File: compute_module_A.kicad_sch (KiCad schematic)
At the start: 4 parts, among them J1 Micro_SD_Card_Det

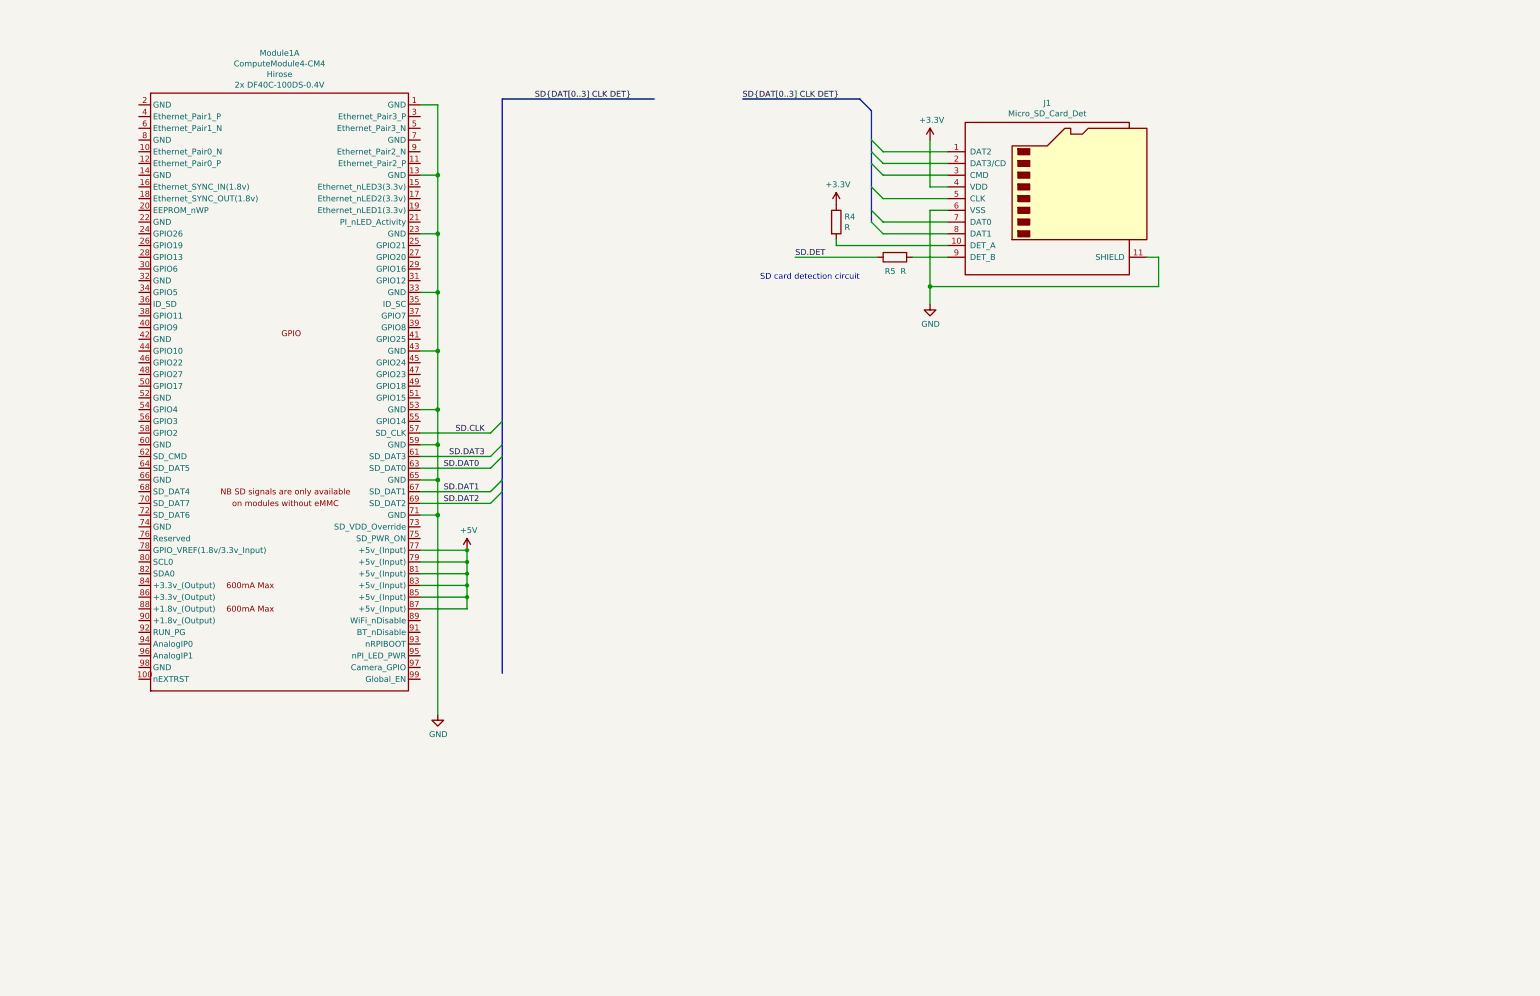
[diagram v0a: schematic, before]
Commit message: Added buses and USB ports to schematic
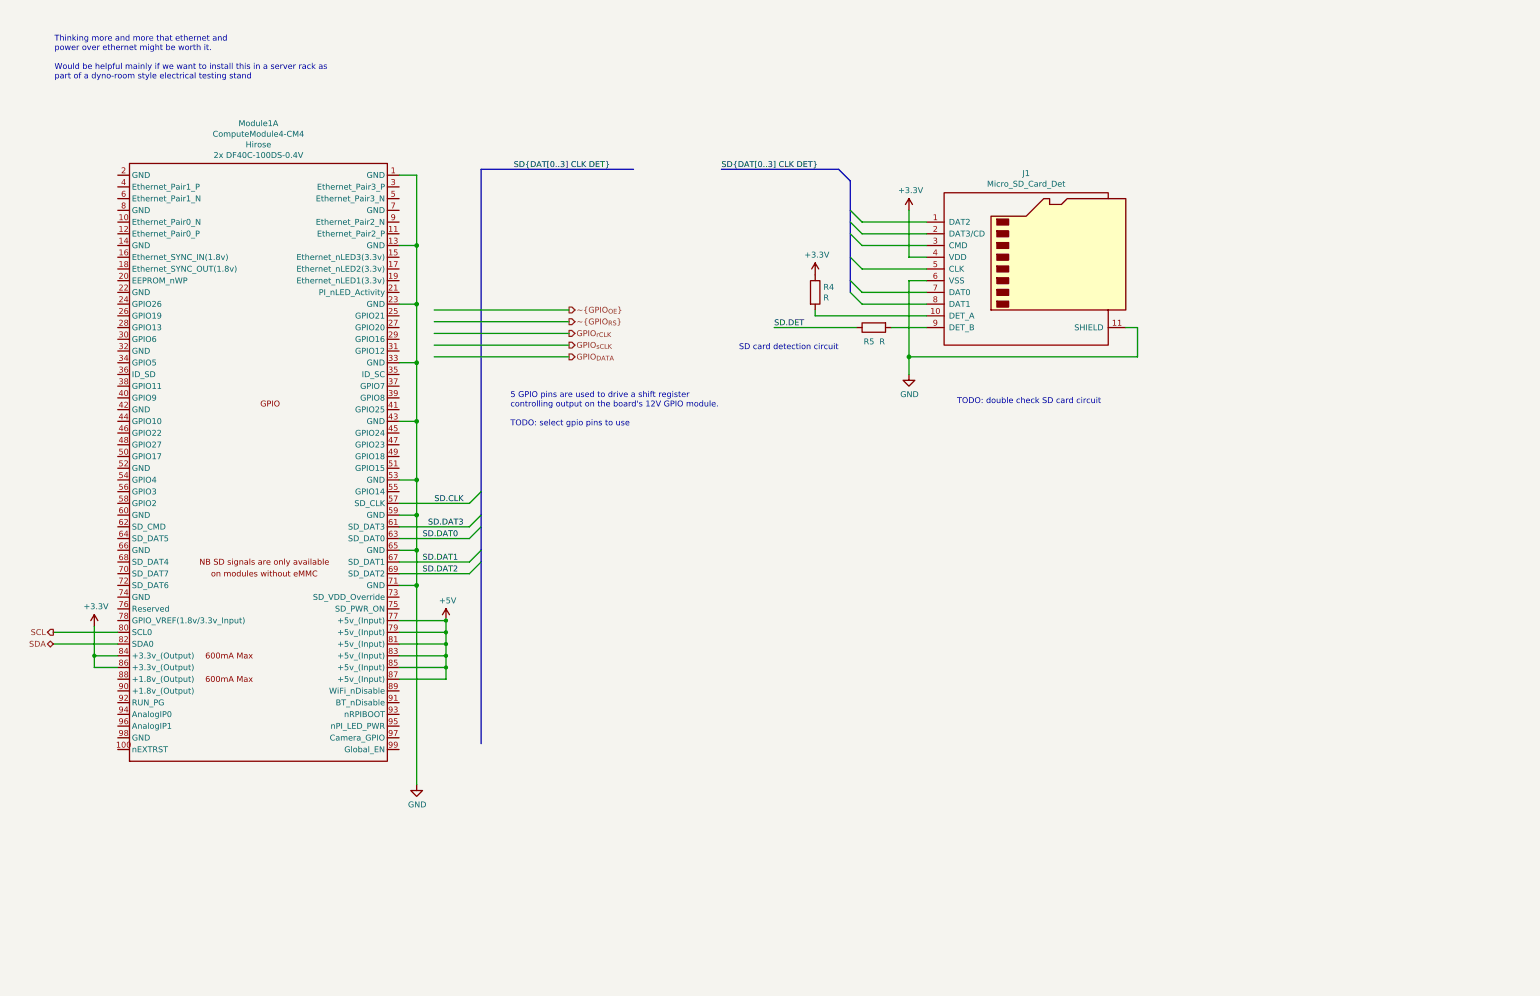
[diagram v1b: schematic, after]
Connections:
- net +3V3: now also Module1.84 (+3.3v_(Output)), Module1.86 (+3.3v_(Output))
- net SCL: now reaches Module1.80 (SCL0)
- net SDA: now reaches Module1.82 (SDA0)
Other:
- note added: "5 GPIO pins are used to drive a shift register controlling output on the board's 12V GPIO module. TODO: select gpio pins to use"
- note added: "TODO: double check SD card circuit"
- note added: "Thinking more and more that ethernet and power over ethernet might be worth it. Would be helpful mainly if we want to install this in a server rack as part of a dyno-room style electrical testing stand"
- company: (none) -> eCafe Racer
- title: (none) -> Dennis
- moved on the sheet: J1, Module1A, R4, R5

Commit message: Added connector for ethernet
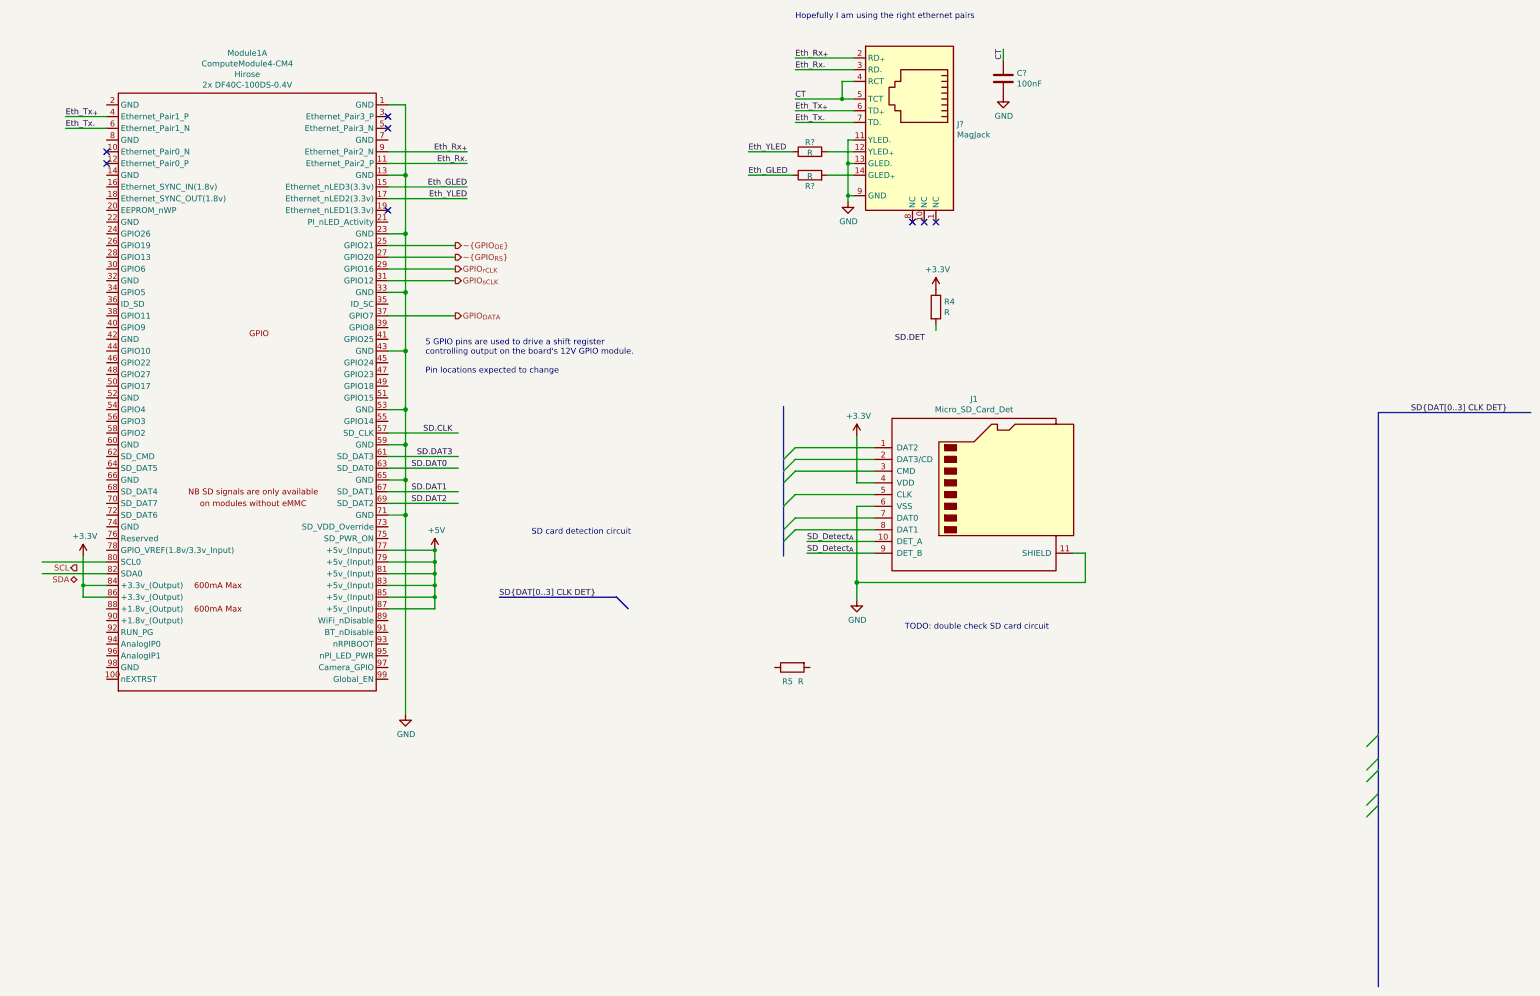
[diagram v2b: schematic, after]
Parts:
- added C?: 100nF, symbol Device:C
- added J?: MagJack, symbol symbols:MagJack
- added R? (x2): R, symbol Device:R
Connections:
- net GND: now also C?.2, J?.11 (YLED_{-}), J?.13 (GLED_{-}), J?.9 (GND)
- net GPIO_{DATA}: now also Module1.37 (GPIO7)
- net GPIO_{rCLK}: now also Module1.29 (GPIO16)
- net GPIO_{sCLK}: now also Module1.31 (GPIO12)
- net SCL: no longer Module1.80 (SCL0)
- net SD.DET: no longer R5.1
- net SDA: no longer Module1.82 (SDA0)
- net ~GPIO_{OE}: now also Module1.25 (GPIO21)
- net ~GPIO_{RS}: now also Module1.27 (GPIO20)
- net at R4.2: no longer J1.10 (DET_A)
- net at R5.2: no longer J1.9 (DET_B)
- net Eth_Rx_{-}: now reaches Module1.11 (Ethernet_Pair2_P)
- net Eth_Rx_{-}: now also J?.3 (RD_{-})
- net Eth_GLED: now reaches Module1.15 (Ethernet_nLED3(3.3v))
- net Eth_GLED: now also R?.1
- net Eth_YLED: now reaches Module1.17 (Ethernet_nLED2(3.3v))
- net Eth_YLED: now also R?.1
- net Eth_Tx_{+}: now reaches Module1.4 (Ethernet_Pair1_P)
- net Eth_Tx_{+}: now also J?.6 (TD_{+})
- net Eth_Tx_{-}: now reaches Module1.6 (Ethernet_Pair1_N)
- net Eth_Tx_{-}: now also J?.7 (TD_{-})
- net Eth_Rx_{+}: now reaches Module1.9 (Ethernet_Pair2_N)
- net Eth_Rx_{+}: now also J?.2 (RD_{+})
- new net: J?.12 (YLED_{+}), R?.2
- new net: J?.14 (GLED_{+}), R?.2
- new net CT: C?.1, J?.4 (RCT), J?.5 (TCT)
- new net SD_Detect_{A}: J1.10 (DET_A), J1.9 (DET_B)
- no-connect marks 0 -> 8
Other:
- note added: "5 GPIO pins are used to drive a shift register controlling output on the board's 12V GPIO module. Pin locations expected to change"
- note added: "Hopefully I am using the right ethernet pairs"
- note removed: "5 GPIO pins are used to drive a shift register controlling output on the board's 12V GPIO module. TODO: select gpio pins to use"
- note removed: "Thinking more and more that ethernet and power over ethernet might be worth it. Would be helpful mainly if we want to install this in a server rack as part of a dyno-room style electrical testing stand"
- moved on the sheet: J1, Module1A, R4, R5

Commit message: SD card circuits
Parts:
- added C10, C12, C13: C, symbol Device:C
- added D2: LED, symbol Device:LED
- added R37, R38: R, symbol Device:R
- added U8: RT9742GGJ5, Package_TO_SOT_SMD:SOT-23-5, symbol symbols:RT9742GGJ5
- gave numbers to parts that had none: 4
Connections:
- net +3V3: now also Module1.78 (GPIO_VREF(1.8v/3.3v_Input)), C10.1, C12.1, R37.1, R38.1, U8.5 (Vin); no longer J1.4 (VDD)
- net GND: now also Module1.7 (GND), C10.2, C12.2, C13.2, U8.2 (GND)
- net SCL: now also Module1.80 (SCL0)
- net SD.CLK: now also J1.5 (CLK)
- net SD.DAT0: now also J1.7 (DAT0)
- net SD.DAT1: now also J1.8 (DAT1)
- net SD.DAT2: now also J1.1 (DAT2)
- net SD.DAT3: now also J1.2 (DAT3/CD)
- net SD.DET: now also Module1.76 (Reserved), R5.1
- net SDA: now also Module1.82 (SDA0)
- net SD_Detect_{A}: now also R4.2; no longer J1.10 (DET_A), J1.9 (DET_B)
- net SD_Detect_{B}: now reaches R5.2
- net SD.CMD: now reaches J1.3 (CMD)
- net SD.CMD: now also Module1.62 (SD_CMD)
- net SD.EN: now reaches Module1.75 (SD_PWR_ON)
- net SD.EN: now also R37.2, U8.4 (EN)
- new net: D2.2 (A), R38.2
- new net SD.Detect_{A}: J1.10 (DET_A)
- new net SD.Detect_{B}: J1.9 (DET_B)
- new net SD.POWER: C13.1, U8.1 (Vout)
- new net SD.power: J1.4 (VDD)
- new net switch_fault: D2.1 (K), U8.3 (~FLG)
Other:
- note added: "Near J1"
- note added: "Near U8"
- note added: "Pin locations expected to change"
- note added: "SD card detection circuit Copied from CM4 io board"
- note removed: "5 GPIO pins are used to drive a shift register controlling output on the board's 12V GPIO module. Pin locations expected to change"
- note removed: "SD card detection circuit"
- note removed: "TODO: double check SD card circuit"
- moved on the sheet: C11, J1, J9, Module1A, R35, R36, R4, R5

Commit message: footprints
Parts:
- C10: renamed from C12; footprint (none) -> Capacitor_SMD:C_0805_2012Metric
- C11: renamed from C13; footprint (none) -> Capacitor_SMD:C_0805_2012Metric
- C12: renamed from C10; footprint (none) -> Capacitor_SMD:C_0805_2012Metric
- C13: renamed from C11; value 100nF -> C; footprint (none) -> Capacitor_SMD:C_0805_2012Metric
- J6: renamed from J9; footprint (none) -> footprints:Molex-0936358314
- J7: renamed from J1; symbol Connector:Micro_SD_Card_Det -> symbols:Micro_SD_Card_Det; Manufacturer (none) -> Molex; Manufacturer Part (none) -> 5031821852; Vendor (none) -> Digikey; Vendor Partt (none) -> WM12834CT-ND
- R10: renamed from R5; footprint (none) -> Resistor_SMD:R_0805_2012Metric
- R11: renamed from R35; footprint (none) -> Resistor_SMD:R_0805_2012Metric
- R12: renamed from R36; footprint (none) -> Resistor_SMD:R_0805_2012Metric
- R13: renamed from R37; footprint (none) -> Resistor_SMD:R_0805_2012Metric
- R14: renamed from R38; footprint (none) -> Resistor_SMD:R_0805_2012Metric
- R9: renamed from R4; footprint (none) -> Resistor_SMD:R_0805_2012Metric
- renumbered D2 to D1, U8 to U4
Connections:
- net SPI.CLK: now reaches Module1.39 (GPIO8)
- net SPI.MOSI: now reaches Module1.41 (GPIO25)
- net SPI.MISO: now reaches Module1.45 (GPIO24)
- net SPI.~CS_{CAN}: now reaches Module1.47 (GPIO23)
- net ~INT_{CAN}: now reaches Module1.49 (GPIO18)
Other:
- note added: "TODO: make or find SD card footprint"
- note added: "This could be on any of the GPIO pins as well"

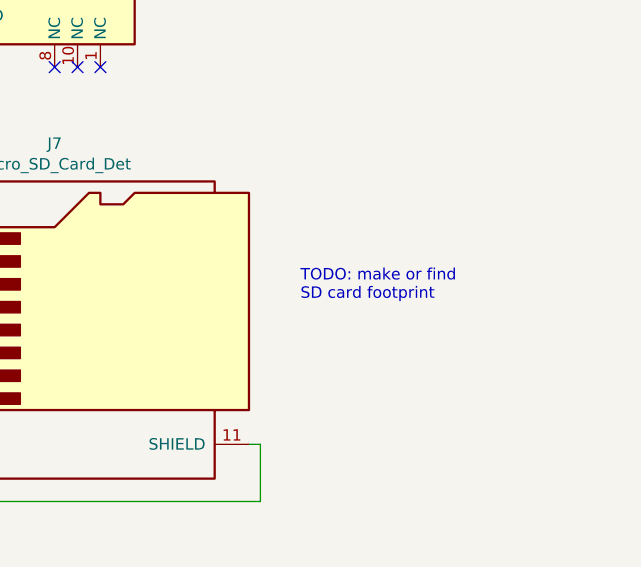
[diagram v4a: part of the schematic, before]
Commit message: Adding footprints and step files for connectors
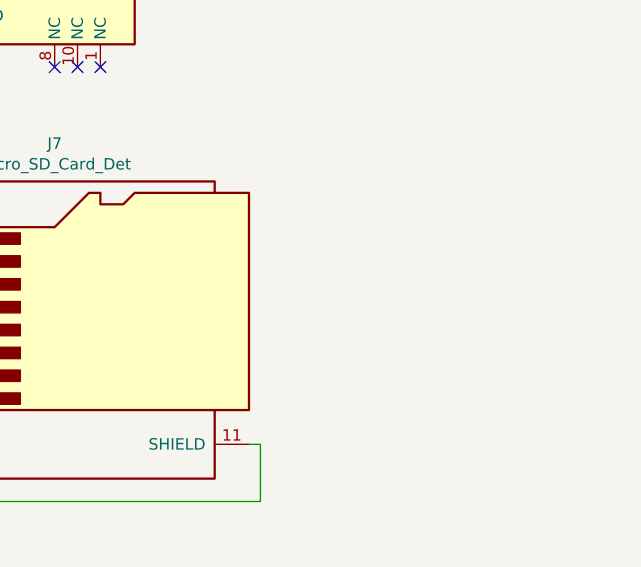
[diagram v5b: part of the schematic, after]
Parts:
- J7: footprint (none) -> Connector_Card:microSD_HC_Hirose_DM3D-SF; Manufacturer Molex -> Hirose Electric Co Ltd; Manufacturer Part 5031821852 -> DM3D-SF
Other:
- note removed: "TODO: make or find SD card footprint"
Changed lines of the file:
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@@
   (junction (at 184.785 53.975) (diameter 0.9144) (color 0 0 0 0))
   (junction (at 184.785 60.96) (diameter 0.9144) (color 0 0 0 0))
+  (no_connect (at 94.615 62.23))
+  (no_connect (at 33.655 52.07))
   (no_connect (at 94.615 44.45))
+  (no_connect (at 203.835 66.675))
   (no_connect (at 198.755 66.675))
+  (no_connect (at 201.295 66.675))
   (no_connect (at 33.655 49.53))
-  (no_connect (at 94.615 62.23))
-  (no_connect (at 201.295 66.675))
   (no_connect (at 94.615 41.91))
-  (no_connect (at 203.835 66.675))
-  (no_connect (at 33.655 52.07))
   (wire (pts (xy 20.955 133.35) (xy 33.655 133.35))
     (stroke (width 0) (type solid) (color 0 0 0 0))
@@
   )
   (text "Hopefully I am using the right ethernet pairs" (at 173.355 22.86 0)
-    (effects (font (size 1.27 1.27)) (justify left bottom))
-  )
-  (text "TODO: make or find \nSD card footprint" (at 226.06 92.71 0)
     (effects (font (size 1.27 1.27)) (justify left bottom))
   )
@@
     (property "Reference" "J7" (id 0) (at 198.755 75.1648 0))
     (property "Value" "Micro_SD_Card_Det" (id 1) (at 198.755 77.4635 0))
-    (property "Footprint" "" (id 2) (at 252.095 78.105 0)
-      (effects (font (size 1.27 1.27)) hide)
-    )
-    (property "Datasheet" "https://www.hirose.com/product/en/download_file/key_name/DM3/category/Catalog/doc_file_id/49662/?file_category_id=4&item_id=195&is_series=1" (id 3) (at 200.025 93.345 0)
+    (property "Footprint" "Connector_Card:microSD_HC_Hirose_DM3D-SF" (id 2) (at 252.095 78.105 0)
+      (effects (font (size 1.27 1.27)) hide)
+    )
+    (property "Datasheet" "https://www.hirose.com/product/document?clcode=CL0609-0033-6-00&productname=DM3AT-SF-PEJ2M5&series=DM3&documenttype=Catalog&lang=en&documentid=D49662_en" (id 3) (at 200.025 93.345 0)
       (effects (font (size 1.27 1.27)) hide)
     )
@@
       (effects (font (size 1.27 1.27)) hide)
     )
-    (property "Manufacturer" "Molex" (id 6) (at 200.025 95.885 0)
-      (effects (font (size 1.27 1.27)) hide)
-    )
-    (property "Manufacturer Part" "5031821852" (id 7) (at 200.025 95.885 0)
-      (effects (font (size 1.27 1.27)) hide)
-    )
+    (property "Manufacturer" "Hirose Electric Co Ltd" (id 6) (at 200.025 95.885 0)
+      (effects (font (size 1.27 1.27)) hide)
+    )
+    (property "Manufacturer Part" "DM3D-SF" (id 7) (at 200.025 95.885 0)
+      (effects (font (size 1.27 1.27)) hide)
+    )
